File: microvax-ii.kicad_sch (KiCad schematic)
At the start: 0 parts

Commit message: Progress on recreating sheet 1.1
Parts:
- added E25: 74LS04, symbol 74xx:74LS04
- added E32: 74F04, symbol 74xx:74LS04
- added E37: 74F32, symbol 74xx:74LS32
- added E38: 74F02, symbol 74xx:7402
- added R1: 47 5% 1/4W, symbol Device:R_US
- added U1: ~, Package_LCC:PLCC-68_SMD-Socket, symbol microvax:78032
- added U2: ~, Package_LCC:PLCC-68_SMD-Socket, symbol microvax:78132
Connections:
- new net: E25.10, U1.4 (IRQ2)
- new net: U1.17 (CLKI), U2.14 (CLKI)
- new net: E38.13, U1.19 (RDY)
- new net: U1.23 (EPS), U2.54 (EPS)
- new net: E25.4, U1.3 (IRQ3)
- new net: E25.8, U1.6 (IRQ1)
- new net: E25.6, U1.8 (PWRFL)
- new net: E37.5, R1.2
- new net +5VD: U1.2 (VDD), U1.32 (VDD), U1.44 (VDD), U1.61 (VDD), U2.11 (VDD), U2.12 (VDD), U2.13 (VDD), U2.35 (VDD), U2.46 (VDD), U2.47 (VDD), U2.48 (VDD), U2.68 (VDD)
- new net BuVAS: E32.11, E32.12
- new net BuVCLKO: E37.6
- new net CS0: U1.26 (CS0)
- new net CS1: U1.25 (CS1)
- new net CS2: U1.24 (CS2)
- new net FSTRDY: E38.11
- new net GND: R1.1, U1.1 (GND), U1.31 (GND), U1.43 (GND), U1.5 (TEST), U1.60 (GND), U2.1 (GND), U2.17 (GND), U2.18 (GND), U2.2 (GND), U2.23 (GND), U2.24 (GND), U2.33 (GND), U2.34 (GND), U2.45 (VBB), U2.52 (GND), U2.53 (GND)
- new net INITRQ: U1.18 (DMR)
- new net IntervalTimer: U1.10 (INTTIM)
- new net READY: E38.12
- new net RIRQ_5: E25.9
- new net RIRQ_6: E25.11
- new net RIRQ_7: E25.3
- new net RPOK: E25.5
- new net uVAS: E32.13, U1.30 (AS)
- new net uVBM0: U1.15 (BM0)
- new net uVBM1: U1.14 (BM1)
- new net uVBM2: U1.13 (BM2)
- new net uVBM3: U1.12 (BM3)
- new net uVBR_14: U1.7 (IRQ0)
- new net uVCLKO: E37.4, U1.27 (CLK0)
- new net uVDBE: U1.28 (DBE)
- new net uVDS: U1.29 (DS)
- new net uVERR: U1.20 (ERR)
- new net uVHALT: U1.11 (HALT)
- new net uVRESET: U1.16 (RESET), U2.16 (RESET)
- new net uVWR: E32.8
- new net ~{BuVAS}: E32.10
- new net ~{uVWR}: E32.9, U1.21 (WR), U2.55 (WR)
- no-connect marks 0 -> 1

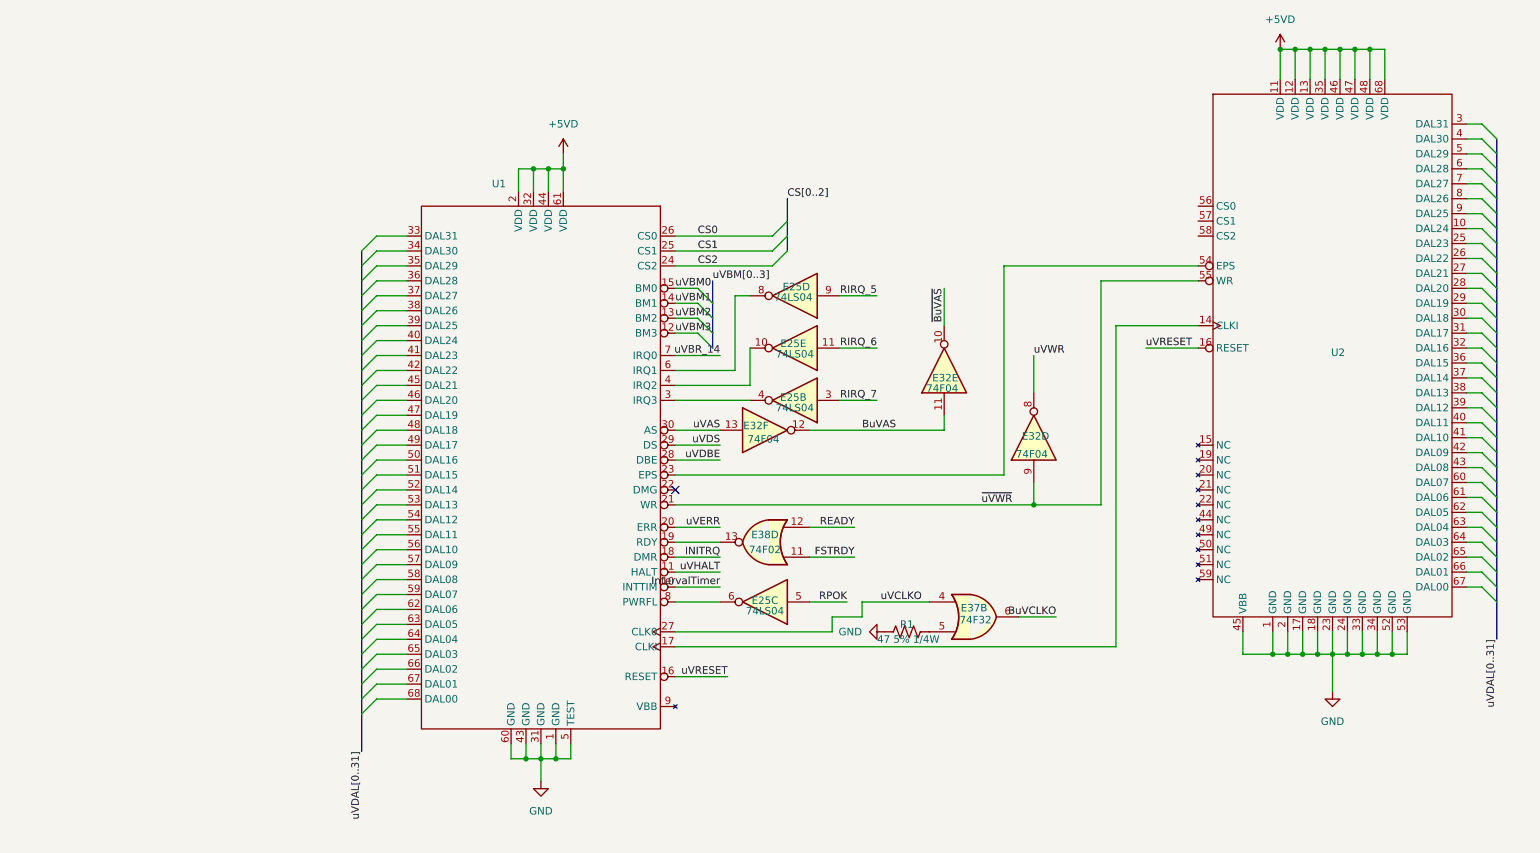
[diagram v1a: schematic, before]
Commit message: Fanout bus correctly
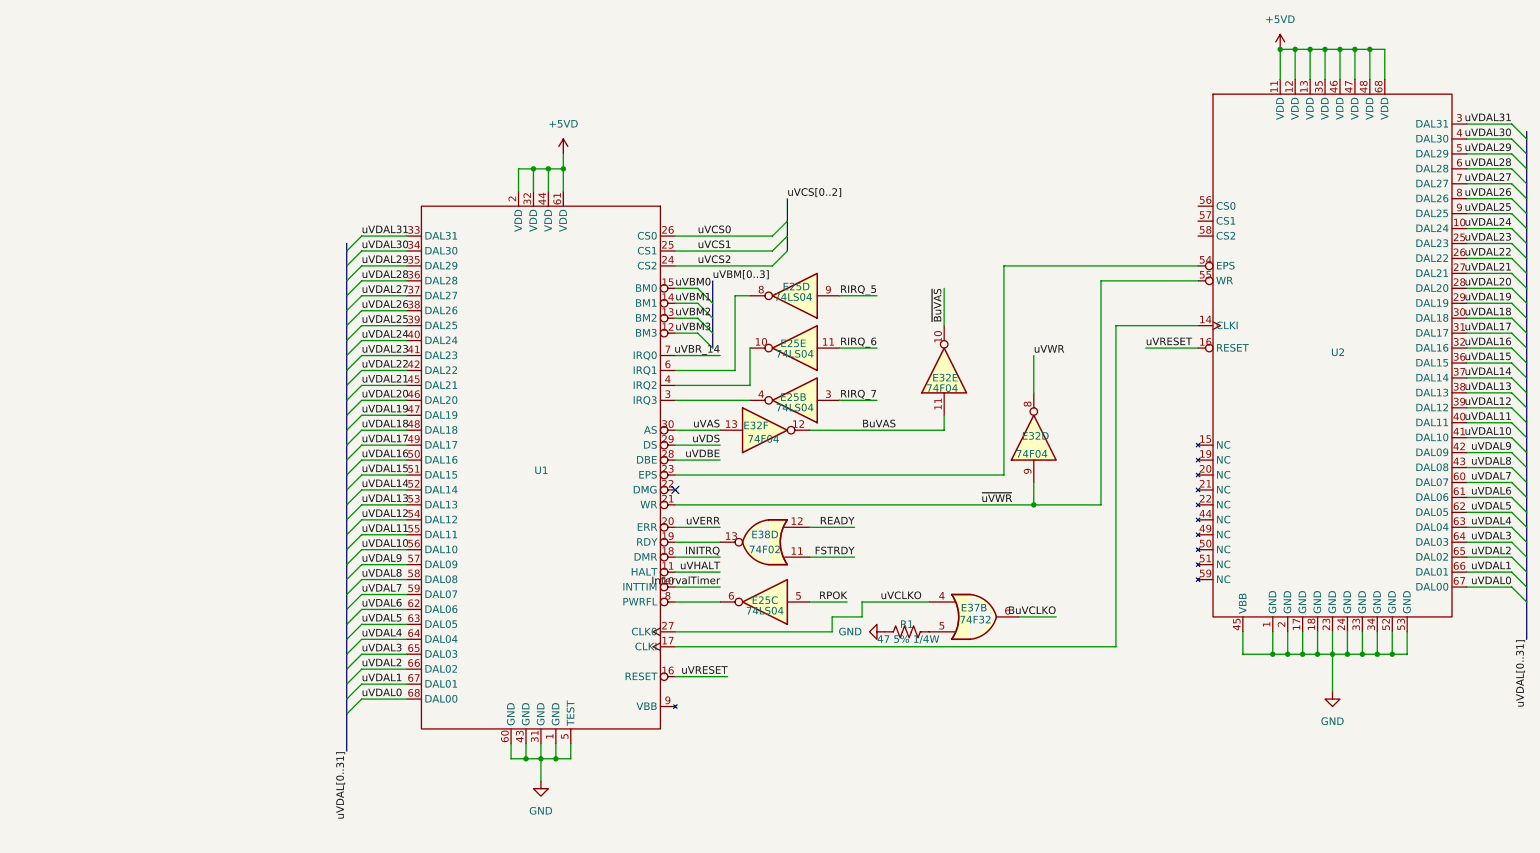
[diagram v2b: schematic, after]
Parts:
- added unit 5 of E32
- added unit 6 of E32
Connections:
- net BuVAS: now also E32.11, E32.12; no longer E32.11, E32.12
- net uVAS: now also E32.13; no longer E32.13
- net ~{BuVAS}: now also E32.10; no longer E32.10
- net uVDAL31: now reaches U1.33 (DAL31)
- net uVDAL31: now also U2.3 (DAL31)
- net uVDAL30: now reaches U1.34 (DAL30)
- net uVDAL30: now also U2.4 (DAL30)
- net uVDAL29: now reaches U1.35 (DAL29)
- net uVDAL29: now also U2.5 (DAL29)
- net uVDAL28: now reaches U1.36 (DAL28)
- net uVDAL28: now also U2.6 (DAL28)
- net uVDAL27: now reaches U1.37 (DAL27)
- net uVDAL27: now also U2.7 (DAL27)
- net uVDAL26: now reaches U1.38 (DAL26)
- net uVDAL26: now also U2.8 (DAL26)
- net uVDAL25: now reaches U1.39 (DAL25)
- net uVDAL25: now also U2.9 (DAL25)
- net uVDAL24: now reaches U1.40 (DAL24)
- net uVDAL24: now also U2.10 (DAL24)
- net uVDAL23: now reaches U1.41 (DAL23)
- net uVDAL23: now also U2.25 (DAL23)
- net uVDAL22: now reaches U1.42 (DAL22)
- net uVDAL22: now also U2.26 (DAL22)
- net uVDAL21: now reaches U1.45 (DAL21)
- net uVDAL21: now also U2.27 (DAL21)
- net uVDAL20: now reaches U1.46 (DAL20)
- net uVDAL20: now also U2.28 (DAL20)
- net uVDAL19: now reaches U1.47 (DAL19)
- net uVDAL19: now also U2.29 (DAL19)
- net uVDAL18: now reaches U1.48 (DAL18)
- net uVDAL18: now also U2.30 (DAL18)
- net uVDAL17: now reaches U1.49 (DAL17)
- net uVDAL17: now also U2.31 (DAL17)
- net uVDAL16: now reaches U1.50 (DAL16)
- net uVDAL16: now also U2.32 (DAL16)
- net uVDAL15: now reaches U1.51 (DAL15)
- net uVDAL15: now also U2.36 (DAL15)
- net uVDAL14: now reaches U1.52 (DAL14)
- net uVDAL14: now also U2.37 (DAL14)
- net uVDAL13: now reaches U1.53 (DAL13)
- net uVDAL13: now also U2.38 (DAL13)
- net uVDAL12: now reaches U1.54 (DAL12)
- net uVDAL12: now also U2.39 (DAL12)
- net uVDAL11: now reaches U1.55 (DAL11)
- net uVDAL11: now also U2.40 (DAL11)
- net uVDAL10: now reaches U1.56 (DAL10)
- net uVDAL10: now also U2.41 (DAL10)
- net uVDAL9: now reaches U1.57 (DAL09)
- net uVDAL9: now also U2.42 (DAL09)
- net uVDAL8: now reaches U1.58 (DAL08)
- net uVDAL8: now also U2.43 (DAL08)
- net uVDAL7: now reaches U1.59 (DAL07)
- net uVDAL7: now also U2.60 (DAL07)
- net uVDAL6: now reaches U1.62 (DAL06)
- net uVDAL6: now also U2.61 (DAL06)
- net uVDAL5: now reaches U1.63 (DAL05)
- net uVDAL5: now also U2.62 (DAL05)
- net uVDAL4: now reaches U1.64 (DAL04)
- net uVDAL4: now also U2.63 (DAL04)
- net uVDAL3: now reaches U1.65 (DAL03)
- net uVDAL3: now also U2.64 (DAL03)
- net uVDAL2: now reaches U1.66 (DAL02)
- net uVDAL2: now also U2.65 (DAL02)
- net uVDAL1: now reaches U1.67 (DAL01)
- net uVDAL1: now also U2.66 (DAL01)
- net uVDAL0: now reaches U1.68 (DAL00)
- net uVDAL0: now also U2.67 (DAL00)
- net CS0 renamed uVCS0
- net CS1 renamed uVCS1
- net CS2 renamed uVCS2

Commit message: Finish memory and start on FPGA
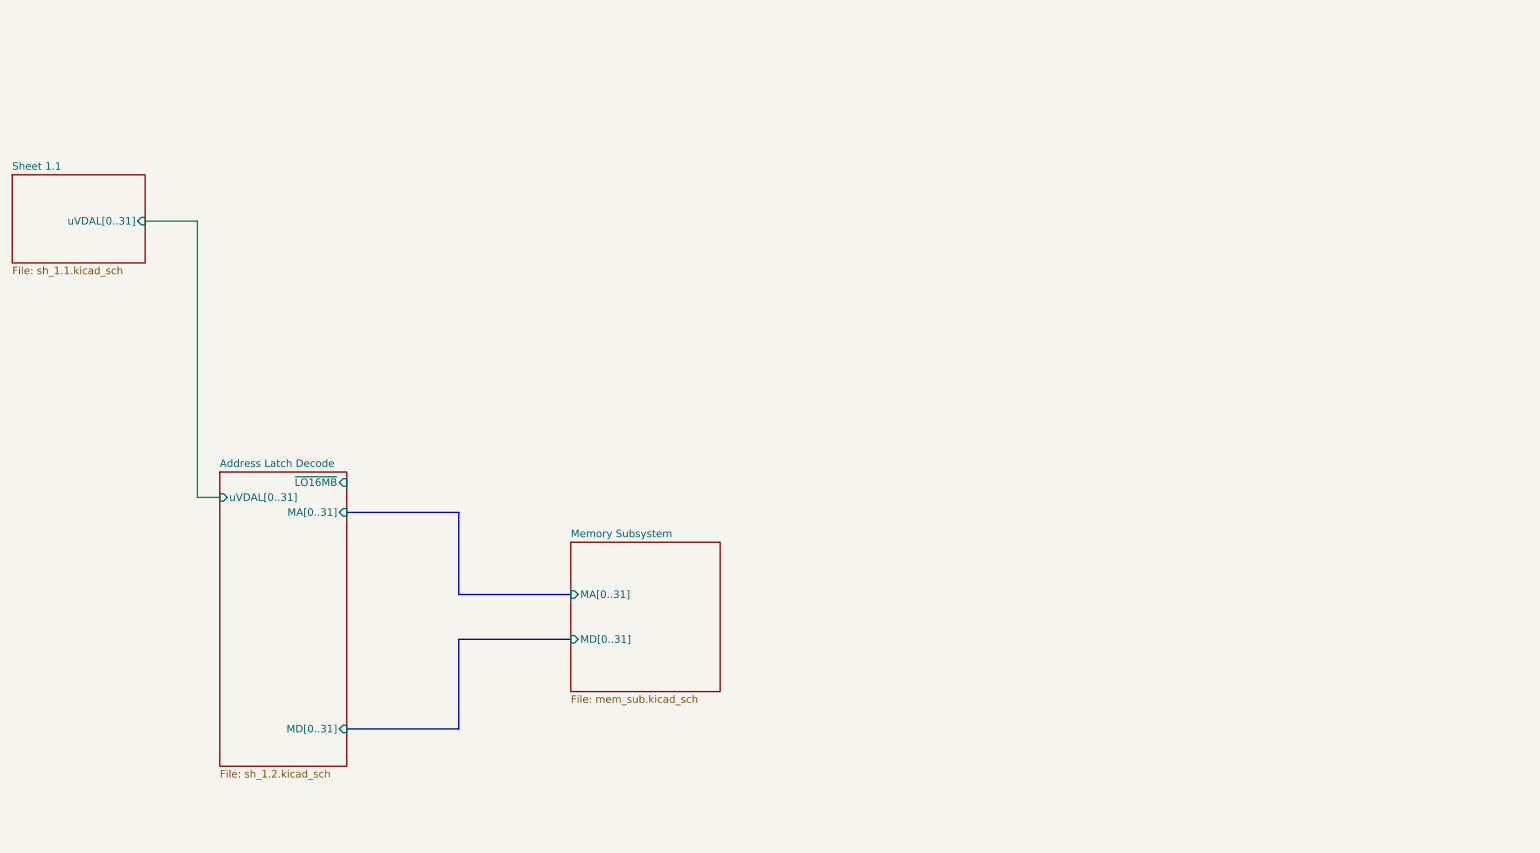
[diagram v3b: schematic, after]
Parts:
- removed E25: 74LS04, symbol 74xx:74LS04
- removed E32: 74F04, symbol 74xx:74LS04
- removed E37: 74F32, symbol 74xx:74LS32
- removed E38: 74F02, symbol 74xx:7402
- removed R1: 47 5% 1/4W, symbol Device:R_US
- removed U1: ~, Package_LCC:PLCC-68_SMD-Socket, symbol microvax:78032
- removed U2: ~, Package_LCC:PLCC-68_SMD-Socket, symbol microvax:78132
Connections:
- no-connect marks 1 -> 0
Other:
- added sheet Address Latch Decode (sh_1.2.kicad_sch)
- added sheet Memory Subsystem (mem_sub.kicad_sch)
- added sheet Sheet 1.1 (sh_1.1.kicad_sch)
